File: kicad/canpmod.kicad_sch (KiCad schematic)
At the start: 12 parts, among them J1 Conn_01x02, J2 PMOD, U1 SN65HVD230

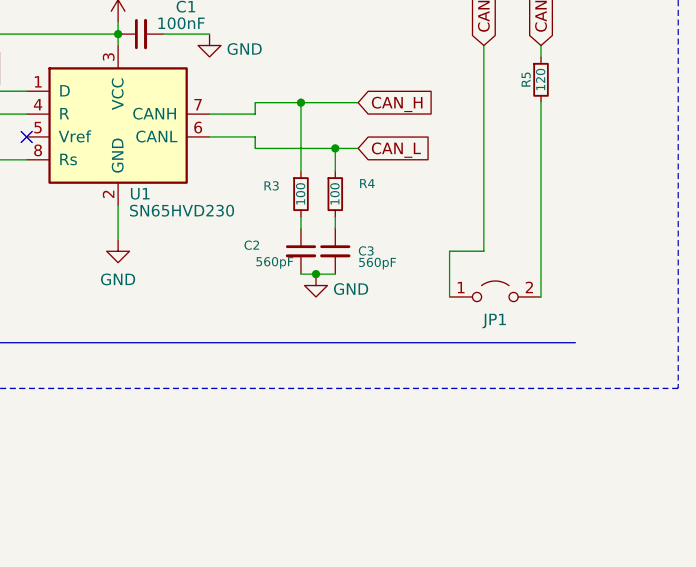
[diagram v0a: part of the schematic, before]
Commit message: Update project to Kicad 9
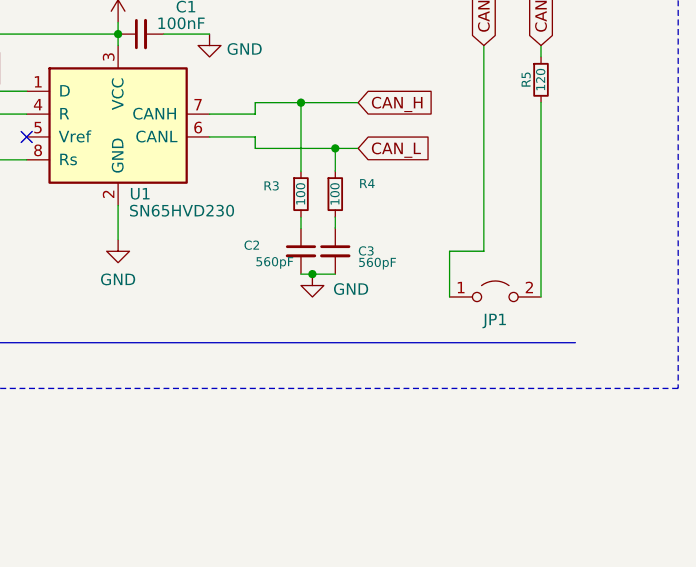
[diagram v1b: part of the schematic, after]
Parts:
- J1: footprint TerminalBlock:TerminalBlock_bornier-2_P5.08mm -> canpmod:TerminalBlock_bornier-2_P5.08mm
- J2: footprint Connector_PinHeader_2.54mm:PinHeader_2x06_P2.54mm_Horizontal -> canpmod:PMOD_2x06_Horizontal
